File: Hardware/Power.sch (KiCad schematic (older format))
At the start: 20 parts

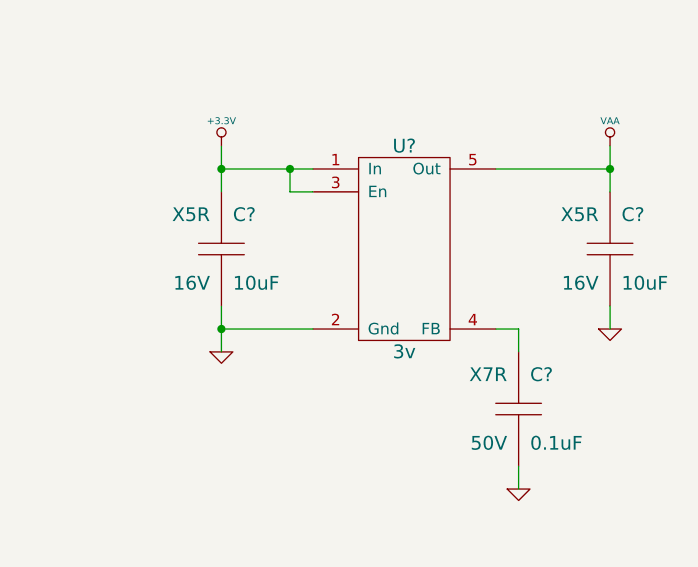
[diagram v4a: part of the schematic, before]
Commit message: Change to STM32L151C
Closes #7
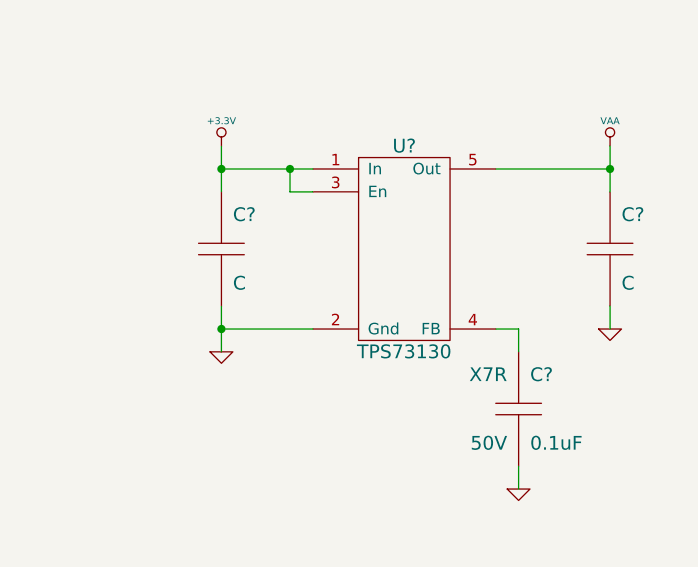
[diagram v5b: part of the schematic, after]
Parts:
- removed C? (x2): 10uF, ~, symbol C
- added C? (x2): C, ~, symbol C
- U?: value 3v -> TPS73130
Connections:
- net +3.3V: now also C?.1
- net GND: now also C?.2, C?.2
- net VAA: now also C?.1
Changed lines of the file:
@@
 Sheet 5 5
 Title ""
-Date "24 sep 2014"
+Date "25 sep 2014"
 Rev ""
 Comp ""
@@
 P 7400 2150
 F 0 "U?" H 7400 2600 60  0000 C CNN
-F 1 "3v" H 7400 1700 60  0000 C CNN
+F 1 "TPS73130" H 7400 1700 60  0000 C CNN
 F 2 "" H 7400 2150 60  0000 C CNN
 F 3 "" H 7400 2150 60  0000 C CNN
@@
 F 6 "296-15804-1-ND" H 7400 2150 60  0001 C CNN "Distributor Part No"
 	1    7400 2150
-	1    0    0    -1
-$EndComp
-$Comp
-L C C?
-U 1 1 5421D961
-P 8300 2150
-F 0 "C?" H 8350 2300 60  0000 L CNN
-F 1 "10uF" H 8350 2000 60  0000 L CNN
-F 2 "~" H 8300 2150 60  0000 C CNN
-F 3 "~" H 8300 2150 60  0000 C CNN
-F 4 "Taiyo Yuden" H 8300 2150 60  0001 C CNN "MFR Name"
-F 5 "EMK212BJ106KG-T" H 8300 2150 60  0001 C CNN "MFR Part No"
-F 6 "587-1295-1-ND" H 8300 2150 60  0001 C CNN "Distributor Part No"
-F 7 "16V" H 8250 2000 60  0000 R CNN "Voltage"
-F 8 "X5R" H 8250 2300 60  0000 R CNN "Dielectric"
-	1    8300 2150
-	1    0    0    -1
-$EndComp
-$Comp
-L C C?
-U 1 1 5421D96C
-P 6600 2150
-F 0 "C?" H 6650 2300 60  0000 L CNN
-F 1 "10uF" H 6650 2000 60  0000 L CNN
-F 2 "~" H 6600 2150 60  0000 C CNN
-F 3 "~" H 6600 2150 60  0000 C CNN
-F 4 "Taiyo Yuden" H 6600 2150 60  0001 C CNN "MFR Name"
-F 5 "EMK212BJ106KG-T" H 6600 2150 60  0001 C CNN "MFR Part No"
-F 6 "587-1295-1-ND" H 6600 2150 60  0001 C CNN "Distributor Part No"
-F 7 "16V" H 6550 2000 60  0000 R CNN "Voltage"
-F 8 "X5R" H 6550 2300 60  0000 R CNN "Dielectric"
-	1    6600 2150
 	1    0    0    -1
 $EndComp
@@
 	1    0    0    -1
 $EndComp
+$Comp
+L C C?
+U 1 1 5424A758
+P 8300 2150
+F 0 "C?" H 8350 2300 60  0000 L CNN
+F 1 "C" H 8350 2000 60  0000 L CNN
+F 2 "~" H 8300 2150 60  0000 C CNN
+F 3 "~" H 8300 2150 60  0000 C CNN
+F 4 "V" H 8250 2000 60  0001 R CNN "Voltage"
+F 5 "D" H 8250 2300 60  0001 R CNN "Dielectric"
+	1    8300 2150
+	1    0    0    -1
+$EndComp
+$Comp
+L C C?
+U 1 1 5424A760
+P 6600 2150
+F 0 "C?" H 6650 2300 60  0000 L CNN
+F 1 "C" H 6650 2000 60  0000 L CNN
+F 2 "~" H 6600 2150 60  0000 C CNN
+F 3 "~" H 6600 2150 60  0000 C CNN
+F 4 "V" H 6550 2000 60  0001 R CNN "Voltage"
+F 5 "D" H 6550 2300 60  0001 R CNN "Dielectric"
+	1    6600 2150
+	1    0    0    -1
+$EndComp

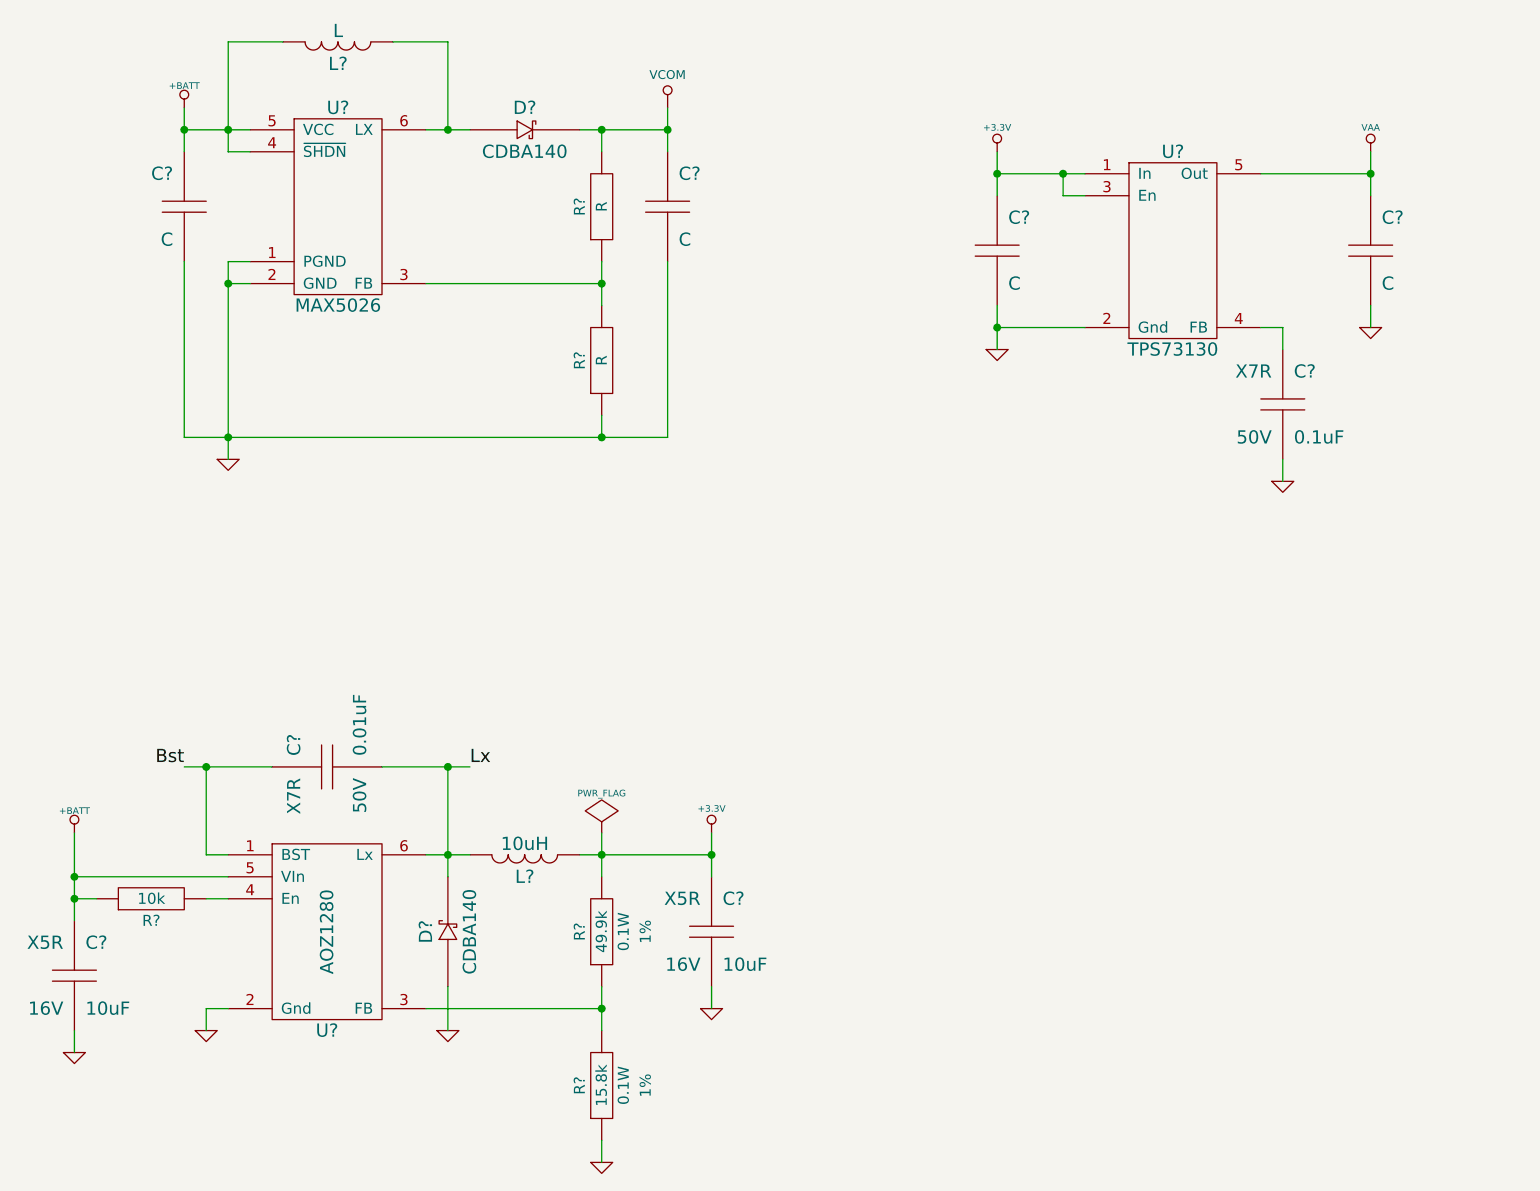
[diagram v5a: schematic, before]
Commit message: Swap to higher voltage 1u cap
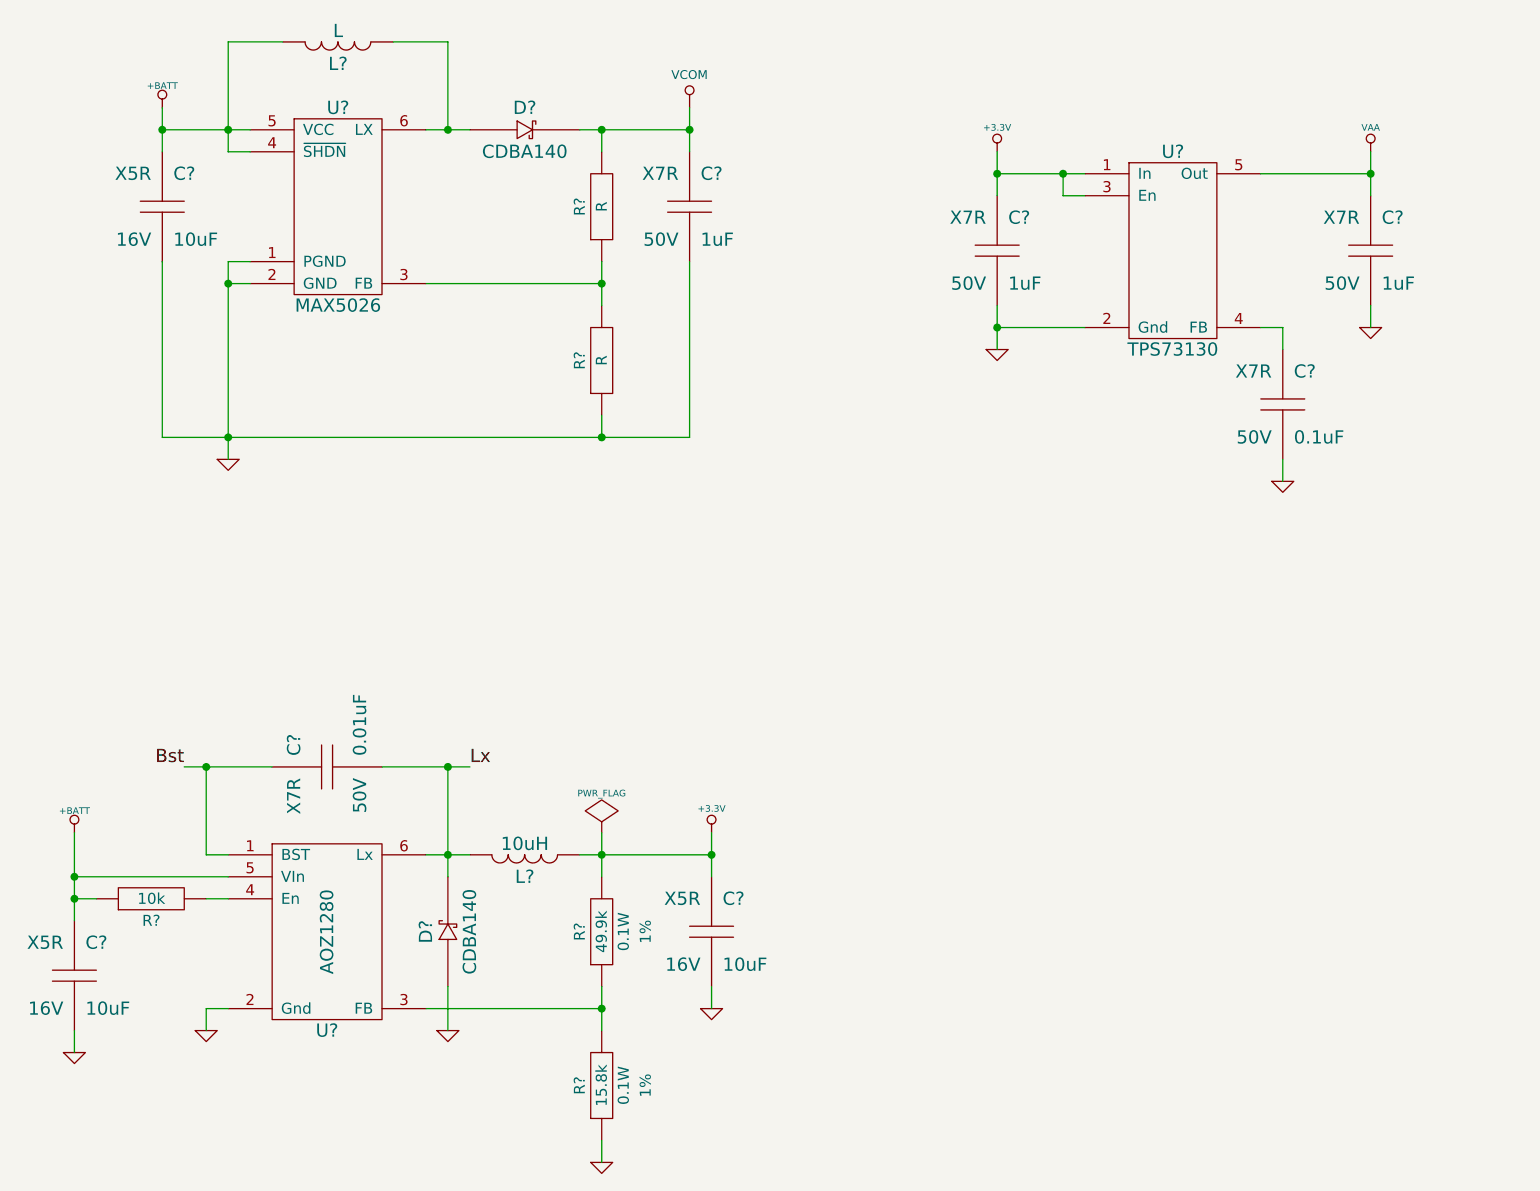
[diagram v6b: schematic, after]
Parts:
- removed C? (x4): C, ~, symbol C
- added C? (x3): 1uF, CAPC1608, symbol C
- added C?: 10uF, ~, symbol C
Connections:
- net +3.3V: now also C?.1
- net +BATT: now also C?.1
- net GND: now also C?.2, C?.2, C?.2, C?.2
- net VAA: now also C?.1
- net VCOM: now also C?.1
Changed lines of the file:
@@
 	3000 4900 3000 4500
 Wire Wire Line
-	2900 4500 3300 4500
-Wire Wire Line
-	4000 4900 4200 4900
-Wire Wire Line
-	3800 4500 4200 4500
-Wire Wire Line
-	4100 4500 4100 5000
+	2900 4500 3000 4500
+Wire Wire Line
+	3000 4500 3300 4500
+Wire Wire Line
+	4000 4900 4100 4900
+Wire Wire Line
+	4100 4900 4200 4900
+Wire Wire Line
+	3800 4500 4100 4500
+Wire Wire Line
+	4100 4500 4200 4500
+Wire Wire Line
+	4100 4500 4100 4900
+Wire Wire Line
+	4100 4900 4100 5000
 Connection ~ 4100 4900
 Wire Wire Line
-	4700 4900 5300 4900
-Wire Wire Line
-	5300 4800 5300 5000
+	4700 4900 4800 4900
+Wire Wire Line
+	4800 4900 5300 4900
+Wire Wire Line
+	5300 4800 5300 4900
+Wire Wire Line
+	5300 4900 5300 5000
 Connection ~ 5300 4900
 Wire Wire Line
-	4800 4800 4800 5000
+	4800 4800 4800 4900
+Wire Wire Line
+	4800 4900 4800 5000
 Connection ~ 4800 4900
 Wire Wire Line
-	4800 5500 4800 5700
+	4800 5500 4800 5600
+Wire Wire Line
+	4800 5600 4800 5700
 Wire Wire Line
 	4000 5600 4800 5600
 Connection ~ 4800 5600
 Wire Wire Line
-	2400 4800 2400 5200
+	2400 4800 2400 5000
+Wire Wire Line
+	2400 5000 2400 5100
+Wire Wire Line
+	2400 5100 2400 5200
 Wire Wire Line
 	3100 5000 2400 5000
@@
 	4100 1200 4100 1600
 Wire Wire Line
-	4000 1600 4200 1600
+	4000 1600 4100 1600
+Wire Wire Line
+	4100 1600 4200 1600
 Wire Wire Line
 	3350 1200 3100 1200
 Wire Wire Line
-	3100 1200 3100 1700
-Wire Wire Line
-	2900 1600 3200 1600
+	3100 1200 3100 1600
+Wire Wire Line
+	3100 1600 3100 1700
+Wire Wire Line
+	2800 1600 3100 1600
+Wire Wire Line
+	3100 1600 3200 1600
 Wire Wire Line
 	3100 1700 3200 1700
@@
 	0    -1   -1   0
 $EndComp
-$Comp
-L C C?
-U 1 1 54209D4A
-P 5100 1950
-F 0 "C?" H 5150 2100 60  0000 L CNN
-F 1 "C" H 5150 1800 60  0000 L CNN
-F 2 "~" H 5100 1950 60  0000 C CNN
-F 3 "~" H 5100 1950 60  0000 C CNN
-F 4 "V" H 5050 1800 60  0001 R CNN "Voltage"
-F 5 "D" H 5050 2100 60  0001 R CNN "Dielectric"
-	1    5100 1950
-	1    0    0    -1
-$EndComp
-$Comp
-L C C?
-U 1 1 54209D9A
-P 2900 1950
-F 0 "C?" H 2950 2100 60  0000 L CNN
-F 1 "C" H 2950 1800 60  0000 L CNN
-F 2 "~" H 2900 1950 60  0000 C CNN
-F 3 "~" H 2900 1950 60  0000 C CNN
-F 4 "V" H 2850 1800 60  0001 R CNN "Voltage"
-F 5 "D" H 2850 2100 60  0001 R CNN "Dielectric"
-	1    2900 1950
-	-1   0    0    -1
-$EndComp
-Wire Wire Line
-	4700 1600 5100 1600
-Wire Wire Line
-	5100 1500 5100 1700
+Wire Wire Line
+	4700 1600 4800 1600
+Wire Wire Line
+	4800 1600 5200 1600
+Wire Wire Line
+	5200 1500 5200 1600
+Wire Wire Line
+	5200 1600 5200 1700
 Wire Wire Line
 	4800 1700 4800 1600
 Connection ~ 4800 1600
 Wire Wire Line
-	4800 2200 4800 2400
+	4800 2200 4800 2300
+Wire Wire Line
+	4800 2300 4800 2400
 Wire Wire Line
 	4000 2300 4800 2300
@@
 $EndComp
 Wire Wire Line
-	3100 2200 3100 3100
-Wire Wire Line
-	2900 3000 5100 3000
+	3100 2200 3100 2300
+Wire Wire Line
+	3100 2300 3100 3000
+Wire Wire Line
+	3100 3000 3100 3100
+Wire Wire Line
+	2800 3000 3100 3000
+Wire Wire Line
+	3100 3000 4800 3000
+Wire Wire Line
+	4800 3000 5200 3000
 Wire Wire Line
 	4800 3000 4800 2900
 Wire Wire Line
-	5100 3000 5100 2200
+	5200 3000 5200 2200
 Connection ~ 4800 3000
 Wire Wire Line
-	2900 2200 2900 3000
+	2800 2200 2800 3000
 Connection ~ 3100 3000
 Wire Wire Line
@@
 Connection ~ 3100 2300
 Wire Wire Line
-	2900 1500 2900 1700
+	2800 1500 2800 1600
+Wire Wire Line
+	2800 1600 2800 1700
 $Comp
 L +BATT #PWR?
 U 1 1 54209FFB
-P 2900 1500
-F 0 "#PWR?" H 2900 1450 20  0001 C CNN
-F 1 "+BATT" H 2900 1600 30  0000 C CNN
-F 2 "" H 2900 1500 60  0000 C CNN
-F 3 "" H 2900 1500 60  0000 C CNN
-	1    2900 1500
-	1    0    0    -1
-$EndComp
-Connection ~ 2900 1600
+P 2800 1500
+F 0 "#PWR?" H 2800 1450 20  0001 C CNN
+F 1 "+BATT" H 2800 1600 30  0000 C CNN
+F 2 "" H 2800 1500 60  0000 C CNN
+F 3 "" H 2800 1500 60  0000 C CNN
+	1    2800 1500
+	1    0    0    -1
+$EndComp
+Connection ~ 2800 1600
 $Comp
 L +BATT #PWR?
@@
 L VCOM #PWR?
 U 1 1 5421D060
-P 5100 1500
-F 0 "#PWR?" H 5100 1700 40  0001 C CNN
-F 1 "VCOM" H 5100 1650 40  0000 C CNN
-F 2 "" H 5100 1500 60  0000 C CNN
-F 3 "" H 5100 1500 60  0000 C CNN
-	1    5100 1500
-	1    0    0    -1
-$EndComp
-Connection ~ 5100 1600
+P 5200 1500
+F 0 "#PWR?" H 5200 1700 40  0001 C CNN
+F 1 "VCOM" H 5200 1650 40  0000 C CNN
+F 2 "" H 5200 1500 60  0000 C CNN
+F 3 "" H 5200 1500 60  0000 C CNN
+	1    5200 1500
+	1    0    0    -1
+$EndComp
+Connection ~ 5200 1600
 $Comp
 L LDO-5 U?
@@
 $EndComp
 Wire Wire Line
-	6600 1700 6600 1900
-Wire Wire Line
-	7000 1800 6600 1800
+	6600 1700 6600 1800
+Wire Wire Line
+	6600 1800 6600 1900
+Wire Wire Line
+	7000 1800 6900 1800
+Wire Wire Line
+	6900 1800 6600 1800
 Connection ~ 6600 1800
 Wire Wire Line
@@
 $EndComp
 Wire Wire Line
-	6600 2400 6600 2600
+	6600 2400 6600 2500
+Wire Wire Line
+	6600 2500 6600 2600
 Wire Wire Line
 	7000 2500 6600 2500
@@
 $EndComp
 Wire Wire Line
-	8300 1700 8300 1900
+	8300 1700 8300 1800
+Wire Wire Line
+	8300 1800 8300 1900
 Wire Wire Line
 	7800 1800 8300 1800
@@
 $Comp
 L C C?
-U 1 1 5424A758
+U 1 1 5424B805
+P 5200 1950
+F 0 "C?" H 5250 2100 60  0000 L CNN
+F 1 "1uF" H 5250 1800 60  0000 L CNN
+F 2 "CAPC1608" H 5200 1950 60  0001 C CNN
+F 3 "~" H 5200 1950 60  0000 C CNN
+F 4 "Samsung" H 5200 1950 60  0001 C CNN "MFR Name"
+F 5 "CL21B105KBFNNNE" H 5200 1950 60  0001 C CNN "MFR Part No"
+F 6 "1276-1029-1-ND" H 5200 1950 60  0001 C CNN "Distributor Part No"
+F 7 "50V" H 5150 1800 60  0000 R CNN "Voltage"
+F 8 "X7R" H 5150 2100 60  0000 R CNN "Dielectric"
+	1    5200 1950
+	1    0    0    -1
+$EndComp
+$Comp
+L C C?
+U 1 1 5424B85F
+P 6600 2150
+F 0 "C?" H 6650 2300 60  0000 L CNN
+F 1 "1uF" H 6650 2000 60  0000 L CNN
+F 2 "CAPC1608" H 6600 2150 60  0001 C CNN
+F 3 "~" H 6600 2150 60  0000 C CNN
+F 4 "Samsung" H 6600 2150 60  0001 C CNN "MFR Name"
+F 5 "CL21B105KBFNNNE" H 6600 2150 60  0001 C CNN "MFR Part No"
+F 6 "1276-1029-1-ND" H 6600 2150 60  0001 C CNN "Distributor Part No"
+F 7 "50V" H 6550 2000 60  0000 R CNN "Voltage"
+F 8 "X7R" H 6550 2300 60  0000 R CNN "Dielectric"
+	1    6600 2150
+	1    0    0    -1
+$EndComp
+$Comp
+L C C?
+U 1 1 5424B86A
 P 8300 2150
 F 0 "C?" H 8350 2300 60  0000 L CNN
-F 1 "C" H 8350 2000 60  0000 L CNN
-F 2 "~" H 8300 2150 60  0000 C CNN
+F 1 "1uF" H 8350 2000 60  0000 L CNN
+F 2 "CAPC1608" H 8300 2150 60  0001 C CNN
 F 3 "~" H 8300 2150 60  0000 C CNN
-F 4 "V" H 8250 2000 60  0001 R CNN "Voltage"
-F 5 "D" H 8250 2300 60  0001 R CNN "Dielectric"
+F 4 "Samsung" H 8300 2150 60  0001 C CNN "MFR Name"
+F 5 "CL21B105KBFNNNE" H 8300 2150 60  0001 C CNN "MFR Part No"
+F 6 "1276-1029-1-ND" H 8300 2150 60  0001 C CNN "Distributor Part No"
+F 7 "50V" H 8250 2000 60  0000 R CNN "Voltage"
+F 8 "X7R" H 8250 2300 60  0000 R CNN "Dielectric"
 	1    8300 2150
 	1    0    0    -1
@@
 $Comp
 L C C?
-U 1 1 5424A760
-P 6600 2150
-F 0 "C?" H 6650 2300 60  0000 L CNN
-F 1 "C" H 6650 2000 60  0000 L CNN
-F 2 "~" H 6600 2150 60  0000 C CNN
-F 3 "~" H 6600 2150 60  0000 C CNN
-F 4 "V" H 6550 2000 60  0001 R CNN "Voltage"
-F 5 "D" H 6550 2300 60  0001 R CNN "Dielectric"
-	1    6600 2150
-	1    0    0    -1
-$EndComp
+U 1 1 5424B875
+P 2800 1950
+F 0 "C?" H 2850 2100 60  0000 L CNN
+F 1 "10uF" H 2850 1800 60  0000 L CNN
+F 2 "~" H 2800 1950 60  0000 C CNN
+F 3 "~" H 2800 1950 60  0000 C CNN
+F 4 "Taiyo Yuden" H 2800 1950 60  0001 C CNN "MFR Name"
+F 5 "EMK212BJ106KG-T" H 2800 1950 60  0001 C CNN "MFR Part No"
+F 6 "587-1295-1-ND" H 2800 1950 60  0001 C CNN "Distributor Part No"
+F 7 "16V" H 2750 1800 60  0000 R CNN "Voltage"
+F 8 "X5R" H 2750 2100 60  0000 R CNN "Dielectric"
+	1    2800 1950
+	1    0    0    -1
+$EndComp
